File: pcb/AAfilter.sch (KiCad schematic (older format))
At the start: 30 parts

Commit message: started assigning footprints
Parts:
- C39, C40, C41, C42, C43, C44, C45, C46, C47, C48, C49, C50: footprint (none) -> Capacitor_SMD:C_0805_2012Metric_Pad1.15x1.40mm_HandSolder
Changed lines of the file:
@@
 F 0 "C51" H 1965 3196 50  0000 L CNN
 F 1 "85p" H 1965 3105 50  0000 L CNN
-F 2 "" H 1888 3000 50  0001 C CNN
+F 2 "Capacitor_SMD:C_0805_2012Metric_Pad1.15x1.40mm_HandSolder" H 1888 3000 50  0001 C CNN
 F 3 "~" H 1850 3150 50  0001 C CNN
 	1    1850 3150
@@
 F 0 "C56" H 2565 3196 50  0000 L CNN
 F 1 "187p" H 2565 3105 50  0000 L CNN
-F 2 "" H 2488 3000 50  0001 C CNN
+F 2 "Capacitor_SMD:C_0805_2012Metric_Pad1.15x1.40mm_HandSolder" H 2488 3000 50  0001 C CNN
 F 3 "~" H 2450 3150 50  0001 C CNN
 	1    2450 3150
@@
 F 0 "C58" H 3165 3196 50  0000 L CNN
 F 1 "187p" H 3165 3105 50  0000 L CNN
-F 2 "" H 3088 3000 50  0001 C CNN
+F 2 "Capacitor_SMD:C_0805_2012Metric_Pad1.15x1.40mm_HandSolder" H 3088 3000 50  0001 C CNN
 F 3 "~" H 3050 3150 50  0001 C CNN
 	1    3050 3150
@@
 F 0 "C61" H 3765 3196 50  0000 L CNN
 F 1 "85p" H 3765 3105 50  0000 L CNN
-F 2 "" H 3688 3000 50  0001 C CNN
+F 2 "Capacitor_SMD:C_0805_2012Metric_Pad1.15x1.40mm_HandSolder" H 3688 3000 50  0001 C CNN
 F 3 "~" H 3650 3150 50  0001 C CNN
 	1    3650 3150
@@
 F 0 "C52" H 1965 3196 50  0000 L CNN
 F 1 "85p" H 1965 3105 50  0000 L CNN
-F 2 "" H 1888 3000 50  0001 C CNN
+F 2 "Capacitor_SMD:C_0805_2012Metric_Pad1.15x1.40mm_HandSolder" H 1888 3000 50  0001 C CNN
 F 3 "~" H 1850 3150 50  0001 C CNN
 	1    1850 3150
@@
 F 0 "C55" H 2565 3196 50  0000 L CNN
 F 1 "187p" H 2565 3105 50  0000 L CNN
-F 2 "" H 2488 3000 50  0001 C CNN
+F 2 "Capacitor_SMD:C_0805_2012Metric_Pad1.15x1.40mm_HandSolder" H 2488 3000 50  0001 C CNN
 F 3 "~" H 2450 3150 50  0001 C CNN
 	1    2450 3150
@@
 F 0 "C59" H 3165 3196 50  0000 L CNN
 F 1 "187p" H 3165 3105 50  0000 L CNN
-F 2 "" H 3088 3000 50  0001 C CNN
+F 2 "Capacitor_SMD:C_0805_2012Metric_Pad1.15x1.40mm_HandSolder" H 3088 3000 50  0001 C CNN
 F 3 "~" H 3050 3150 50  0001 C CNN
 	1    3050 3150
@@
 F 0 "C62" H 3765 3196 50  0000 L CNN
 F 1 "85p" H 3765 3105 50  0000 L CNN
-F 2 "" H 3688 3000 50  0001 C CNN
+F 2 "Capacitor_SMD:C_0805_2012Metric_Pad1.15x1.40mm_HandSolder" H 3688 3000 50  0001 C CNN
 F 3 "~" H 3650 3150 50  0001 C CNN
 	1    3650 3150
@@
 F 0 "C53" H 1965 3196 50  0000 L CNN
 F 1 "85p" H 1965 3105 50  0000 L CNN
-F 2 "" H 1888 3000 50  0001 C CNN
+F 2 "Capacitor_SMD:C_0805_2012Metric_Pad1.15x1.40mm_HandSolder" H 1888 3000 50  0001 C CNN
 F 3 "~" H 1850 3150 50  0001 C CNN
 	1    1850 3150
@@
 F 0 "C54" H 2565 3196 50  0000 L CNN
 F 1 "187p" H 2565 3105 50  0000 L CNN
-F 2 "" H 2488 3000 50  0001 C CNN
+F 2 "Capacitor_SMD:C_0805_2012Metric_Pad1.15x1.40mm_HandSolder" H 2488 3000 50  0001 C CNN
 F 3 "~" H 2450 3150 50  0001 C CNN
 	1    2450 3150
@@
 F 0 "C57" H 3165 3196 50  0000 L CNN
 F 1 "187p" H 3165 3105 50  0000 L CNN
-F 2 "" H 3088 3000 50  0001 C CNN
+F 2 "Capacitor_SMD:C_0805_2012Metric_Pad1.15x1.40mm_HandSolder" H 3088 3000 50  0001 C CNN
 F 3 "~" H 3050 3150 50  0001 C CNN
 	1    3050 3150
@@
 F 0 "C60" H 3765 3196 50  0000 L CNN
 F 1 "85p" H 3765 3105 50  0000 L CNN
-F 2 "" H 3688 3000 50  0001 C CNN
+F 2 "Capacitor_SMD:C_0805_2012Metric_Pad1.15x1.40mm_HandSolder" H 3688 3000 50  0001 C CNN
 F 3 "~" H 3650 3150 50  0001 C CNN
 	1    3650 3150

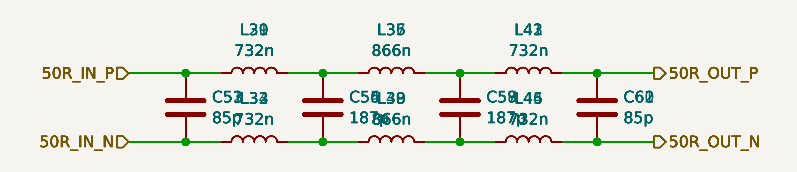
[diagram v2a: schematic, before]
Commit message: Update footprints, move to 0603 passives for JLCPCB assembly, create transformer footprints
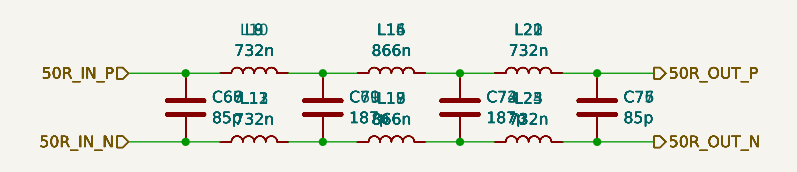
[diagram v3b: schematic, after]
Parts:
- C66: renamed from C39; footprint Capacitor_SMD:C_0805_2012Metric_Pad1.15x1.40mm_HandSolder -> Capacitor_SMD:C_0603_1608Metric
- C67: renamed from C40; footprint Capacitor_SMD:C_0805_2012Metric_Pad1.15x1.40mm_HandSolder -> Capacitor_SMD:C_0603_1608Metric
- C68: renamed from C41; footprint Capacitor_SMD:C_0805_2012Metric_Pad1.15x1.40mm_HandSolder -> Capacitor_SMD:C_0603_1608Metric
- C69: renamed from C42; footprint Capacitor_SMD:C_0805_2012Metric_Pad1.15x1.40mm_HandSolder -> Capacitor_SMD:C_0603_1608Metric
- C70: renamed from C43; footprint Capacitor_SMD:C_0805_2012Metric_Pad1.15x1.40mm_HandSolder -> Capacitor_SMD:C_0603_1608Metric
- C71: renamed from C44; footprint Capacitor_SMD:C_0805_2012Metric_Pad1.15x1.40mm_HandSolder -> Capacitor_SMD:C_0603_1608Metric
- C72: renamed from C45; footprint Capacitor_SMD:C_0805_2012Metric_Pad1.15x1.40mm_HandSolder -> Capacitor_SMD:C_0603_1608Metric
- C73: renamed from C46; footprint Capacitor_SMD:C_0805_2012Metric_Pad1.15x1.40mm_HandSolder -> Capacitor_SMD:C_0603_1608Metric
- C74: renamed from C47; footprint Capacitor_SMD:C_0805_2012Metric_Pad1.15x1.40mm_HandSolder -> Capacitor_SMD:C_0603_1608Metric
- C75: renamed from C48; footprint Capacitor_SMD:C_0805_2012Metric_Pad1.15x1.40mm_HandSolder -> Capacitor_SMD:C_0603_1608Metric
- C76: renamed from C49; footprint Capacitor_SMD:C_0805_2012Metric_Pad1.15x1.40mm_HandSolder -> Capacitor_SMD:C_0603_1608Metric
- C77: renamed from C50; footprint Capacitor_SMD:C_0805_2012Metric_Pad1.15x1.40mm_HandSolder -> Capacitor_SMD:C_0603_1608Metric
- renumbered L13 to L10, L14 to L11, L15 to L12, L16 to L13, L17 to L14, L18 to L15, L19 to L16, L20 to L17, L21 to L18, L22 to L19, L23 to L20, L24 to L21, L25 to L22, L26 to L23, L27 to L24, L28 to L25, L11 to L8, L12 to L9

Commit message: finish up vregs, routed filters, iq baseband outputs
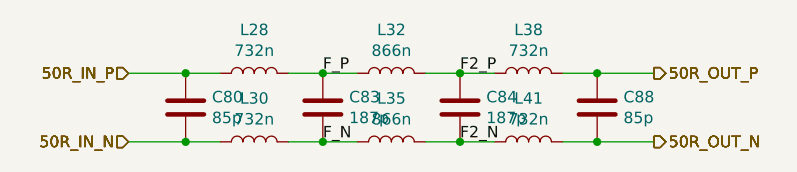
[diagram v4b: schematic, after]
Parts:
- removed C66, C67, C75, C77: 85p, Capacitor_SMD:C_0603_1608Metric, symbol Device:C
- removed C69, C70, C73, C74: 187p, Capacitor_SMD:C_0603_1608Metric, symbol Device:C
- removed L11, L13, L21, L22, L24, L25, L8, L9: 732n, symbol Device:L
- removed L15, L16, L18, L19: 866n, symbol Device:L
- L10, L12, L14, L17, L20, L23: footprint (none) -> Inductor_SMD:L_0603_1608Metric
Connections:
- net F_P: now reaches C71.1, L10.2, L14.1
- net F_N: now reaches C71.2, L12.2, L17.1
- net F2_P: now reaches C72.1, L14.2, L20.1
- net F2_N: now reaches C72.2, L17.2, L23.1

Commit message: routing the dac wires
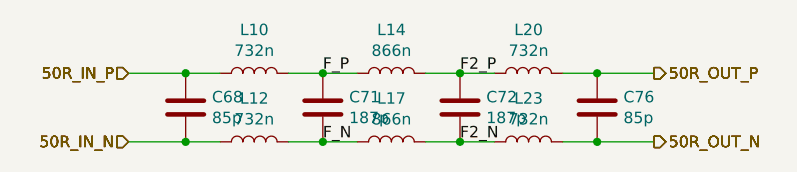
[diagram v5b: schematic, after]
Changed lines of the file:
@@
 $Descr A4 11693 8268
 encoding utf-8
-Sheet 6 7
+Sheet 5 7
 Title ""
 Date ""
@@
 AR Path="/5FB3742F/5FBD65F9/5FBFCF8A" Ref="C?"  Part="1"
 AR Path="/5FB3742F/5FBDAA40/5FBFCF8A" Ref="C88"  Part="1"
-F 0 "C88" H 3765 3196 50  0000 L CNN
+F 0 "C76" H 3765 3196 50  0000 L CNN
 F 1 "85p" H 3765 3105 50  0000 L CNN
 F 2 "Capacitor_SMD:C_0603_1608Metric" H 3688 3000 50  0001 C CNN
@@
 AR Path="/5FB3742F/5FBD65F9/5FBFCF84" Ref="L?"  Part="1"
 AR Path="/5FB3742F/5FBDAA40/5FBFCF84" Ref="L30"  Part="1"
-F 0 "L30" V 2340 3300 50  0000 C CNN
+F 0 "L12" V 2340 3300 50  0000 C CNN
 F 1 "732n" V 2249 3300 50  0000 C CNN
 F 2 "Inductor_SMD:L_0603_1608Metric" H 2150 3300 50  0001 C CNN
@@
 AR Path="/5FB3742F/5FBD65F9/5FBFD013" Ref="C?"  Part="1"
 AR Path="/5FB3742F/5FBDAA40/5FBFD013" Ref="C80"  Part="1"
-F 0 "C80" H 1965 3196 50  0000 L CNN
+F 0 "C68" H 1965 3196 50  0000 L CNN
 F 1 "85p" H 1965 3105 50  0000 L CNN
 F 2 "Capacitor_SMD:C_0603_1608Metric" H 1888 3000 50  0001 C CNN
@@
 AR Path="/5FB3742F/5FBD65F9/5FBFD014" Ref="L?"  Part="1"
 AR Path="/5FB3742F/5FBDAA40/5FBFD014" Ref="L28"  Part="1"
-F 0 "L28" V 2340 3000 50  0000 C CNN
+F 0 "L10" V 2340 3000 50  0000 C CNN
 F 1 "732n" V 2249 3000 50  0000 C CNN
 F 2 "Inductor_SMD:L_0603_1608Metric" H 2150 3000 50  0001 C CNN
@@
 AR Path="/5FB3742F/5FBD65F9/5FBA6C76" Ref="C?"  Part="1"
 AR Path="/5FB3742F/5FBDAA40/5FBA6C76" Ref="C84"  Part="1"
-F 0 "C84" H 3165 3196 50  0000 L CNN
+F 0 "C72" H 3165 3196 50  0000 L CNN
 F 1 "187p" H 3165 3105 50  0000 L CNN
 F 2 "Capacitor_SMD:C_0603_1608Metric" H 3088 3000 50  0001 C CNN
@@
 AR Path="/5FB3742F/5FBD65F9/5FBA6C88" Ref="L?"  Part="1"
 AR Path="/5FB3742F/5FBDAA40/5FBA6C88" Ref="L38"  Part="1"
-F 0 "L38" V 3540 3000 50  0000 C CNN
+F 0 "L20" V 3540 3000 50  0000 C CNN
 F 1 "732n" V 3449 3000 50  0000 C CNN
 F 2 "Inductor_SMD:L_0603_1608Metric" H 3350 3000 50  0001 C CNN
@@
 AR Path="/5FB3742F/5FBD65F9/5FBA6C70" Ref="L?"  Part="1"
 AR Path="/5FB3742F/5FBDAA40/5FBA6C70" Ref="L35"  Part="1"
-F 0 "L35" V 2940 3300 50  0000 C CNN
+F 0 "L17" V 2940 3300 50  0000 C CNN
 F 1 "866n" V 2849 3300 50  0000 C CNN
 F 2 "Inductor_SMD:L_0603_1608Metric" H 2750 3300 50  0001 C CNN
@@
 AR Path="/5FB3742F/5FBD65F9/5FBFD016" Ref="C?"  Part="1"
 AR Path="/5FB3742F/5FBDAA40/5FBFD016" Ref="C83"  Part="1"
-F 0 "C83" H 2565 3196 50  0000 L CNN
+F 0 "C71" H 2565 3196 50  0000 L CNN
 F 1 "187p" H 2565 3105 50  0000 L CNN
 F 2 "Capacitor_SMD:C_0603_1608Metric" H 2488 3000 50  0001 C CNN
@@
 AR Path="/5FB3742F/5FBD65F9/5FBA6C6A" Ref="L?"  Part="1"
 AR Path="/5FB3742F/5FBDAA40/5FBA6C6A" Ref="L32"  Part="1"
-F 0 "L32" V 2940 3000 50  0000 C CNN
+F 0 "L14" V 2940 3000 50  0000 C CNN
 F 1 "866n" V 2849 3000 50  0000 C CNN
 F 2 "Inductor_SMD:L_0603_1608Metric" H 2750 3000 50  0001 C CNN
@@
 AR Path="/5FB3742F/5FBD65F9/5FBA6C7C" Ref="L?"  Part="1"
 AR Path="/5FB3742F/5FBDAA40/5FBA6C7C" Ref="L41"  Part="1"
-F 0 "L41" V 3540 3300 50  0000 C CNN
+F 0 "L23" V 3540 3300 50  0000 C CNN
 F 1 "732n" V 3449 3300 50  0000 C CNN
 F 2 "Inductor_SMD:L_0603_1608Metric" H 3350 3300 50  0001 C CNN

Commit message: routing contiued, add swtiches, remove test points, all parts now positioned on board
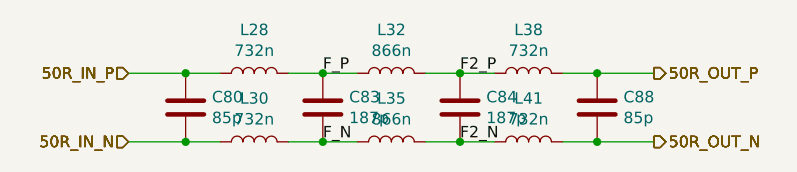
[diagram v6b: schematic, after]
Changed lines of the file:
@@
 $Descr A4 11693 8268
 encoding utf-8
-Sheet 5 7
+Sheet 6 6
 Title ""
 Date ""
@@
 AR Path="/5FB3742F/5FBD65F9/5FBFCF8A" Ref="C?"  Part="1"
 AR Path="/5FB3742F/5FBDAA40/5FBFCF8A" Ref="C88"  Part="1"
-F 0 "C76" H 3765 3196 50  0000 L CNN
+F 0 "C88" H 3765 3196 50  0000 L CNN
 F 1 "85p" H 3765 3105 50  0000 L CNN
 F 2 "Capacitor_SMD:C_0603_1608Metric" H 3688 3000 50  0001 C CNN
@@
 AR Path="/5FB3742F/5FBD65F9/5FBFCF84" Ref="L?"  Part="1"
 AR Path="/5FB3742F/5FBDAA40/5FBFCF84" Ref="L30"  Part="1"
-F 0 "L12" V 2340 3300 50  0000 C CNN
+F 0 "L30" V 2340 3300 50  0000 C CNN
 F 1 "732n" V 2249 3300 50  0000 C CNN
 F 2 "Inductor_SMD:L_0603_1608Metric" H 2150 3300 50  0001 C CNN
@@
 AR Path="/5FB3742F/5FBD65F9/5FBFD013" Ref="C?"  Part="1"
 AR Path="/5FB3742F/5FBDAA40/5FBFD013" Ref="C80"  Part="1"
-F 0 "C68" H 1965 3196 50  0000 L CNN
+F 0 "C80" H 1965 3196 50  0000 L CNN
 F 1 "85p" H 1965 3105 50  0000 L CNN
 F 2 "Capacitor_SMD:C_0603_1608Metric" H 1888 3000 50  0001 C CNN
@@
 AR Path="/5FB3742F/5FBD65F9/5FBFD014" Ref="L?"  Part="1"
 AR Path="/5FB3742F/5FBDAA40/5FBFD014" Ref="L28"  Part="1"
-F 0 "L10" V 2340 3000 50  0000 C CNN
+F 0 "L28" V 2340 3000 50  0000 C CNN
 F 1 "732n" V 2249 3000 50  0000 C CNN
 F 2 "Inductor_SMD:L_0603_1608Metric" H 2150 3000 50  0001 C CNN
@@
 AR Path="/5FB3742F/5FBD65F9/5FBA6C76" Ref="C?"  Part="1"
 AR Path="/5FB3742F/5FBDAA40/5FBA6C76" Ref="C84"  Part="1"
-F 0 "C72" H 3165 3196 50  0000 L CNN
+F 0 "C84" H 3165 3196 50  0000 L CNN
 F 1 "187p" H 3165 3105 50  0000 L CNN
 F 2 "Capacitor_SMD:C_0603_1608Metric" H 3088 3000 50  0001 C CNN
@@
 AR Path="/5FB3742F/5FBD65F9/5FBA6C88" Ref="L?"  Part="1"
 AR Path="/5FB3742F/5FBDAA40/5FBA6C88" Ref="L38"  Part="1"
-F 0 "L20" V 3540 3000 50  0000 C CNN
+F 0 "L38" V 3540 3000 50  0000 C CNN
 F 1 "732n" V 3449 3000 50  0000 C CNN
 F 2 "Inductor_SMD:L_0603_1608Metric" H 3350 3000 50  0001 C CNN
@@
 AR Path="/5FB3742F/5FBD65F9/5FBA6C70" Ref="L?"  Part="1"
 AR Path="/5FB3742F/5FBDAA40/5FBA6C70" Ref="L35"  Part="1"
-F 0 "L17" V 2940 3300 50  0000 C CNN
+F 0 "L35" V 2940 3300 50  0000 C CNN
 F 1 "866n" V 2849 3300 50  0000 C CNN
 F 2 "Inductor_SMD:L_0603_1608Metric" H 2750 3300 50  0001 C CNN
@@
 AR Path="/5FB3742F/5FBD65F9/5FBFD016" Ref="C?"  Part="1"
 AR Path="/5FB3742F/5FBDAA40/5FBFD016" Ref="C83"  Part="1"
-F 0 "C71" H 2565 3196 50  0000 L CNN
+F 0 "C83" H 2565 3196 50  0000 L CNN
 F 1 "187p" H 2565 3105 50  0000 L CNN
 F 2 "Capacitor_SMD:C_0603_1608Metric" H 2488 3000 50  0001 C CNN
@@
 AR Path="/5FB3742F/5FBD65F9/5FBA6C6A" Ref="L?"  Part="1"
 AR Path="/5FB3742F/5FBDAA40/5FBA6C6A" Ref="L32"  Part="1"
-F 0 "L14" V 2940 3000 50  0000 C CNN
+F 0 "L32" V 2940 3000 50  0000 C CNN
 F 1 "866n" V 2849 3000 50  0000 C CNN
 F 2 "Inductor_SMD:L_0603_1608Metric" H 2750 3000 50  0001 C CNN
@@
 AR Path="/5FB3742F/5FBD65F9/5FBA6C7C" Ref="L?"  Part="1"
 AR Path="/5FB3742F/5FBDAA40/5FBA6C7C" Ref="L41"  Part="1"
-F 0 "L23" V 3540 3300 50  0000 C CNN
+F 0 "L41" V 3540 3300 50  0000 C CNN
 F 1 "732n" V 3449 3300 50  0000 C CNN
 F 2 "Inductor_SMD:L_0603_1608Metric" H 3350 3300 50  0001 C CNN
